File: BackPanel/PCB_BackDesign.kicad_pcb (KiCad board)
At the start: 2 copper layers, 62.5 x 32 mm, 29 parts, among them J1 Conn_01x08_Pin, J2 Conn_01x09_Pin, J3 Conn_01x02_Pin, J4 Conn_01x02_Pin, SW1 KS11R23CQD, SW2 KS11R23CQD, SW3 KS11R23CQD

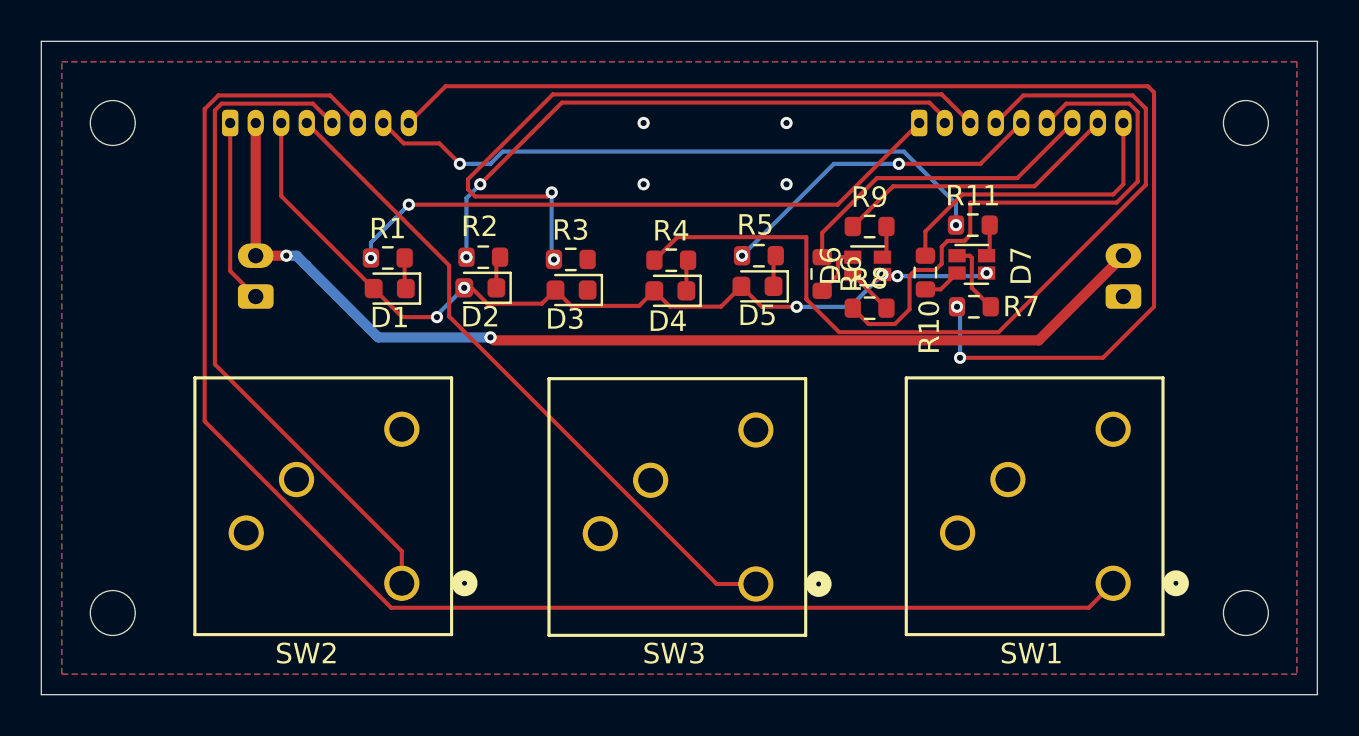
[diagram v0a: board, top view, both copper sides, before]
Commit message: Tidied up some designators; moved two traces on the top layer to pass
DRC.
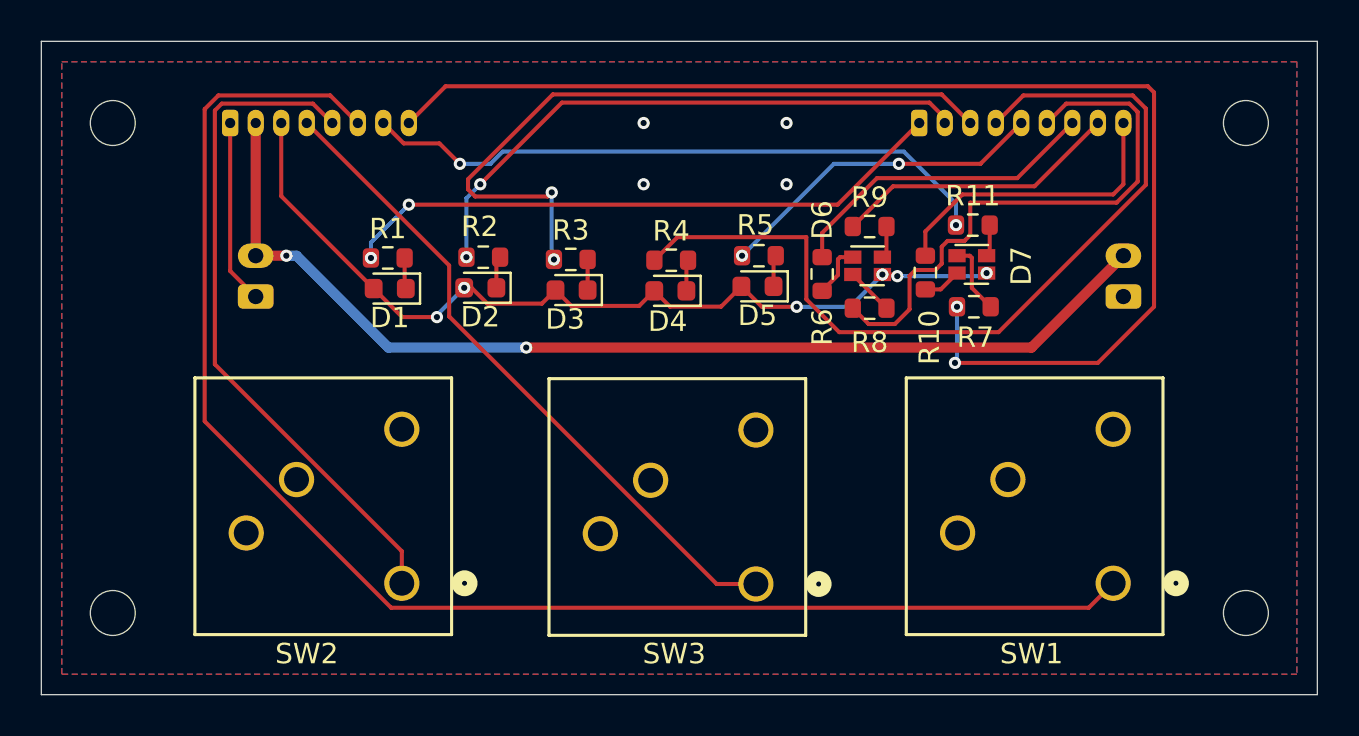
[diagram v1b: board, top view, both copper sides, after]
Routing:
- net Net-(D3-K): track 0.00 -> 1.50 mm
- net /LED6_G: track 61.0 -> 61.6 mm
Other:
- board text added: "NUgus Back Panel IO"
- board text added: "William Burgin - github.com/NUbots/NUware v1.0 - 21/2/2025"
- board text removed: "NUgus Back Panel IO William Burgin - github.com/NUbots/NUware v1.0 - 21/2/2025"
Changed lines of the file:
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@@
 		(tags "resistor")
 		(property "Reference" "R8"
-			(at 0 -1.43 0)
+			(at 0 1.679208 0)
 			(layer "F.SilkS")
 			(effects
@@
 		(tags "LED RGB Chip SMD")
 		(property "Reference" "D6"
-			(at 0 -1.8 90)
+			(at 2.245792 -2.22 90)
 			(layer "F.SilkS")
 			(effects
@@
 		(tags "resistor")
 		(property "Reference" "R7"
-			(at 2.325 0 0)
+			(at 0.075 1.5 0)
 			(layer "F.SilkS")
 			(effects
@@
 		(tags "resistor")
 		(property "Reference" "R6"
-			(at 0 -1.43 90)
+			(at 2.604208 -0.005 90)
 			(layer "F.SilkS")
 			(effects
@@
 		(tags "resistor")
 		(property "Reference" "R10"
-			(at 2.675 -0.19937 90)
+			(at 3.175 -0.19937 90)
 			(layer "F.SilkS")
 			(effects
@@
 		(tags "connector JST PH side entry")
 		(property "Reference" "J4"
-			(at 1 2.9 90)
+			(at -3.25 0 0)
 			(layer "B.SilkS")
 			(effects
@@
 		(tags "connector JST PH side entry")
 		(property "Reference" "J3"
-			(at 1.935596 2.9 90)
+			(at -3.25 0 180)
 			(layer "B.SilkS")
 			(effects
@@
 		(layer "Edge.Cuts")
 	)
-	(gr_text "NUgus Back Panel IO\nWilliam Burgin - github.com/NUbots/NUware\nv1.0 - 21/2/2025"
-		(at 114 74.5 90)
+	(gr_text "NUgus Back Panel IO"
+		(at 141 78.75 0)
 		(layer "B.SilkS")
 		(effects
 			(font
-				(size 0.5 0.5)
-				(thickness 0.1)
+				(size 2 2)
+				(thickness 0.3)
 			)
-			(justify left bottom mirror)
+			(justify bottom mirror)
+		)
+	)
+	(gr_text "William Burgin - github.com/NUbots/NUware\nv1.0 - 21/2/2025"
+		(at 141 82.75 0)
+		(layer "B.SilkS")
+		(effects
+			(font
+				(size 1 1)
+				(thickness 0.15)
+			)
+			(justify bottom mirror)
 		)
 	)
@@
 	)
 	(segment
+		(start 136.2575 79.1825)
+		(end 136.2575 77.6825)
+		(width 0.2)
+		(layer "F.Cu")
+		(net 4)
+	)
+	(segment
 		(start 141.095157 77.8025)
 		(end 141.177657 77.72)
@@
 	)
 	(segment
-		(start 158.354208 81.645792)
-		(end 131.645792 81.645792)
+		(start 162.5 77.5)
+		(end 158 82)
 		(width 0.5)
 		(layer "F.Cu")
@@
 	)
 	(segment
-		(start 131.645792 81.645792)
-		(end 131.5 81.5)
-		(width 0.2)
-		(layer "F.Cu")
-		(net 13)
-	)
-	(segment
-		(start 162.5 77.5)
-		(end 158.354208 81.645792)
+		(start 158 82)
+		(end 133.25 82)
 		(width 0.5)
 		(layer "F.Cu")
@@
 	)
 	(via
-		(at 131.5 81.5)
+		(at 133.25 82)
 		(size 0.6)
 		(drill 0.3)
@@
 	)
 	(segment
-		(start 122 77.5)
-		(end 121.5 77.5)
+		(start 133.25 82)
+		(end 126.5 82)
 		(width 0.5)
 		(layer "B.Cu")
@@
 	)
 	(segment
-		(start 126 81.5)
-		(end 122.5 78)
+		(start 122 77.5)
+		(end 121.5 77.5)
 		(width 0.5)
 		(layer "B.Cu")
@@
 	)
 	(segment
-		(start 122.5 78)
+		(start 126.5 82)
 		(end 122 77.5)
 		(width 0.5)
@@
 	)
 	(segment
-		(start 131.5 81.5)
-		(end 126 81.5)
-		(width 0.5)
-		(layer "B.Cu")
-		(net 13)
-	)
-	(segment
-		(start 164 80)
-		(end 161.5 82.5)
+		(start 129.3 69.2)
+		(end 127.5 71)
 		(width 0.2)
 		(layer "F.Cu")
@@
 	)
 	(segment
-		(start 164 69.5)
+		(start 161.25 82.75)
 		(end 164 80)
 		(width 0.2)
@@
 	)
 	(segment
-		(start 163.7 69.2)
-		(end 164 69.5)
+		(start 154.25 82.75)
+		(end 161.25 82.75)
 		(width 0.2)
 		(layer "F.Cu")
@@
 	)
 	(segment
-		(start 127.5 71)
+		(start 163.7 69.2)
 		(end 129.3 69.2)
 		(width 0.2)
@@
 	)
 	(segment
-		(start 129.3 69.2)
-		(end 163.7 69.2)
+		(start 164 80)
+		(end 164 69.5)
 		(width 0.2)
 		(layer "F.Cu")
@@
 	)
 	(segment
-		(start 161.5 82.5)
-		(end 154.5 82.5)
+		(start 164 69.5)
+		(end 163.7 69.2)
 		(width 0.2)
 		(layer "F.Cu")
@@
 	)
 	(via
-		(at 154.5 82.5)
+		(at 154.25 82.75)
 		(size 0.6)
 		(drill 0.3)
@@
 	)
 	(segment
-		(start 154.5 80.15)
-		(end 154.35 80)
+		(start 154.25 82.75)
+		(end 154.35 82.65)
 		(width 0.2)
 		(layer "B.Cu")
@@
 	)
 	(segment
-		(start 154.5 82.5)
-		(end 154.5 80.15)
+		(start 154.35 82.65)
+		(end 154.35 80)
 		(width 0.2)
 		(layer "B.Cu")

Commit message: Added three debouncing capacitors.
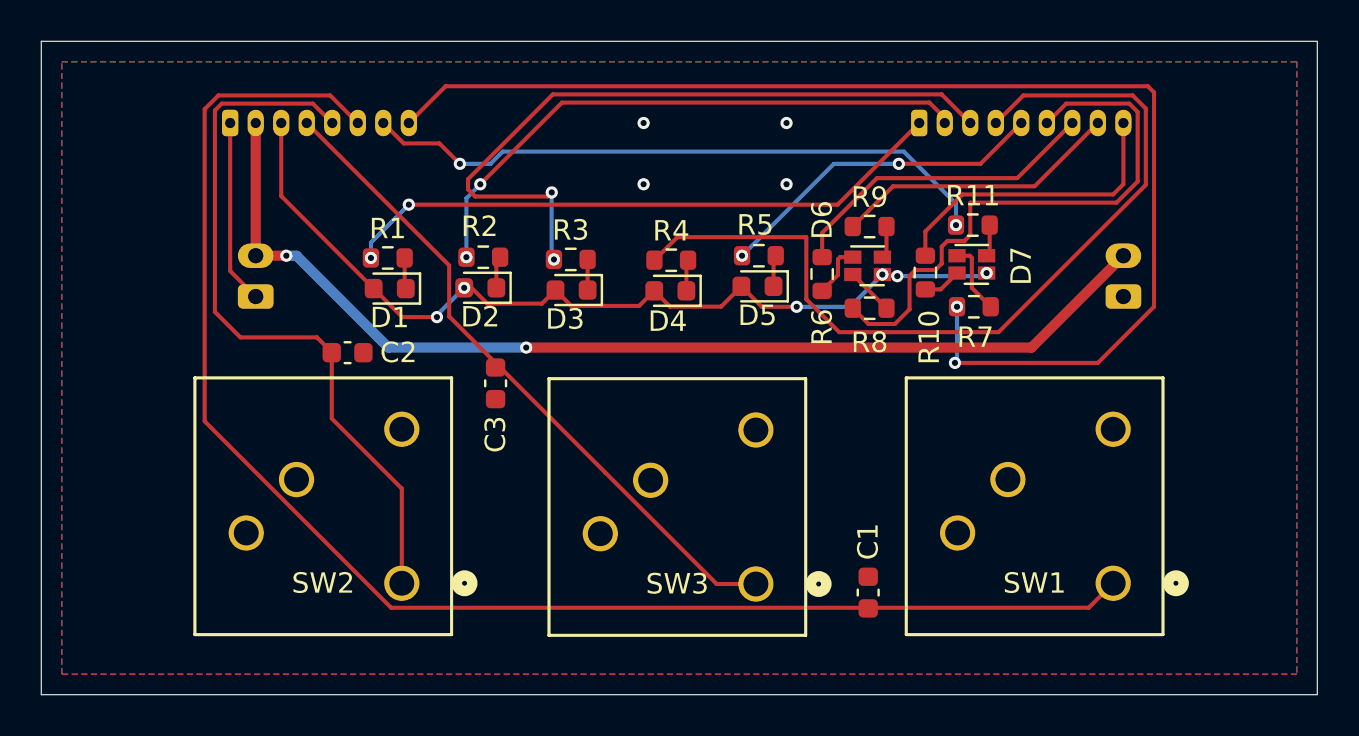
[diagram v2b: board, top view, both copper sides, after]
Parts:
- removed REF** (x4): MountingHole_2.2mm_M2, MountingHole:MountingHole_2.2mm_M2
- added C1: 100nF, Capacitor_SMD:C_0603_1608Metric, F.Cu at (150.0, 94.0)
- added C2: 100nF, Capacitor_SMD:C_0603_1608Metric, F.Cu at (124.5, 82.2)
- added C3: 100nF, Capacitor_SMD:C_0603_1608Metric, F.Cu at (131.8, 83.8)
- D1, D2: value LED -> LED (yellow-green) 5988060107F
- D3: value LED -> LED (red) 5988010107F
- D4: value LED -> LED (blue) 5988091107F
- D5: value LED -> LED (green) 5988070107F
- D6, D7: value LED_RGBA -> EAST1616RGBB2
- J1: value Conn_01x08_Pin -> Molex Picoblade 0530470810
- J2: value Conn_01x09_Pin -> Molex Picoblade 0530470910
- J3, J4: value Conn_01x02_Pin -> B2B-PH-K-S
- R1, R10, R2, R3, R8: value 470OHM -> 470Ω
- R11, R4, R5, R6, R7, R9: value 470OHM -> 240Ω
- SW1: value KS11R23CQD -> KS11R23CQD (red)
- SW2: value KS11R23CQD -> KS11R22CQD (black)
- SW3: value KS11R23CQD -> KS11R27CQD (blue)
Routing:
- net /SW_MODE: track 33.2 -> 35.4 mm
